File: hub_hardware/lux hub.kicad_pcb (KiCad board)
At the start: 4 copper layers, 105.4 x 54.6 mm, 136 parts, among them CON1 48V, CON2 USB-MINI-B, P1 CONN_4, P2 CONN_4, P3 CONN_4, P4 CONN_4, P5 CONN_4, P6 CONN_4, P7 CONN_4, Q1 DMP6023LE-13, Q10 BC856BLT, Q11 BTX54CTU, Q12 BC856BLT, Q13 BTX54CTU, Q2 BC856BLT, Q3 BTX54CTU, Q4 BC856BLT, Q5 BTX54CTU, Q6 BC856BLT, Q7 BTX54CTU, Q8 BC856BLT, Q9 BTX54CTU, SW1 BOOT, U1 3V3REG, U10 ISL83485IBZ, U11 2CH-TVS, U12 ISL83485IBZ, U13 2CH-TVS, U14 ISL83485IBZ, U15 2CH-TVS, U2 STM32F042-32, U3 4068, U4 ISL83485IBZ, U5 2CH-TVS, U6 ISL83485IBZ, U7 2CH-TVS, U8 ISL83485IBZ, U9 2CH-TVS

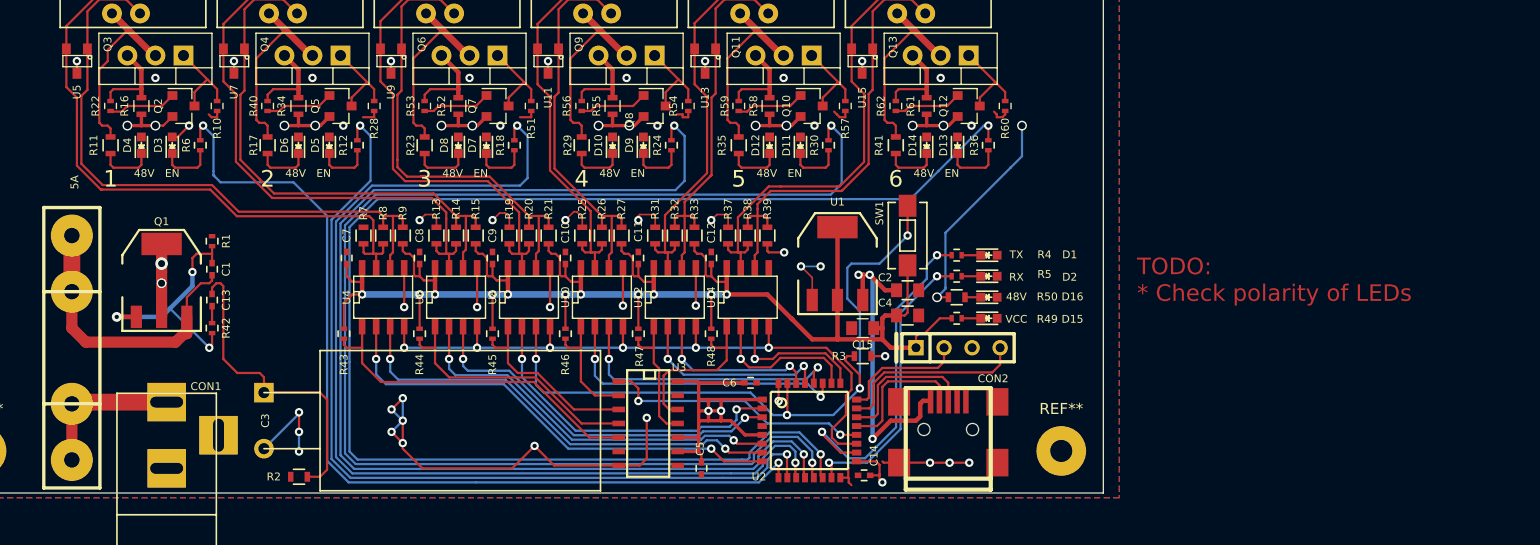
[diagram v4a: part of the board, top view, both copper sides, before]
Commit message: WIP Lux Hub v7; need to re-route 1W 2512 resistors
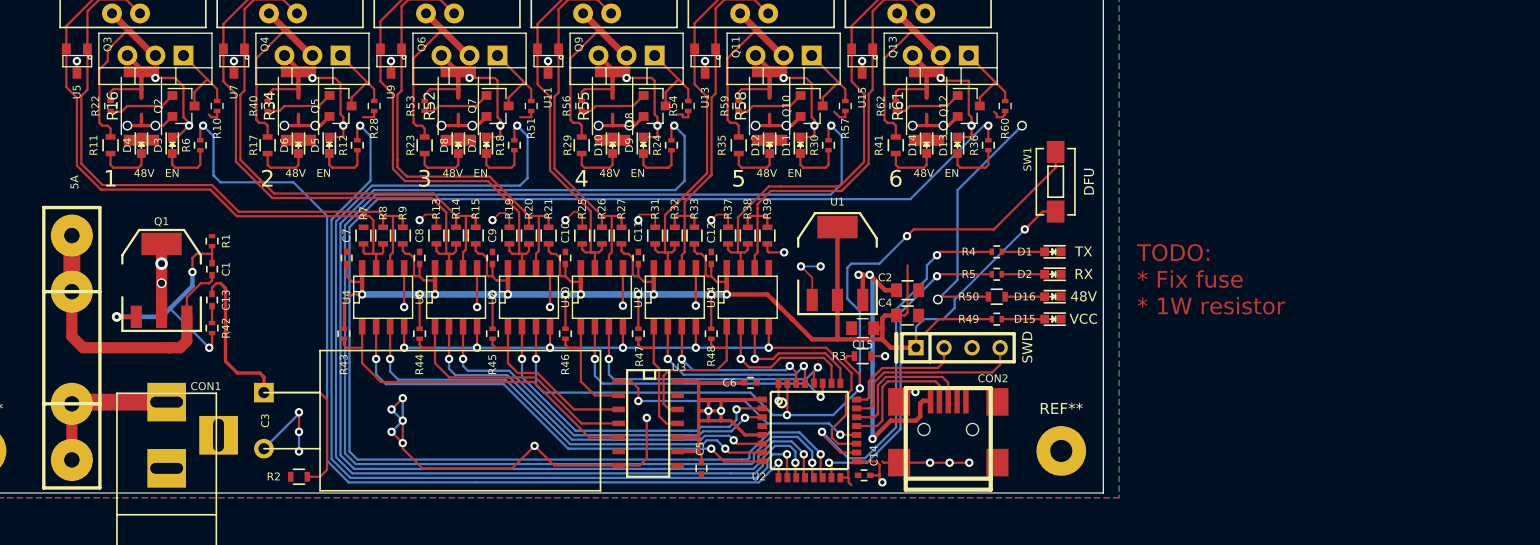
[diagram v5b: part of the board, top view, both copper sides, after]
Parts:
- D1, D10, D11, D12, D13, D14, D15, D16, D2, D3, D4, D5, D6, D7, D8, D9: footprint LEDs:LED_0603 -> custom:LED_0603_flipped
- R16, R34, R52, R55, R58, R61: footprint Resistors_SMD:R_0603 -> Resistors_SMD:R_2512
- moved SW1 14.3 mm to (125.2, 96.3)
- moved D1 5.80 mm to (125.0, 102.6)
- moved D2 5.79 mm to (125.0, 104.6)
- moved D15 5.79 mm to (125.0, 108.7)
- moved D16 5.79 mm to (125.0, 106.7)
- moved R4 3.64 mm to (119.9, 102.6)
- moved R5 3.64 mm to (119.9, 104.6)
- moved R49 3.63 mm to (119.9, 108.7)
- moved R50 3.63 mm to (119.9, 106.7)
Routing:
- net GND: track 117.3 -> 171.5 mm, vias 34 -> 46
- net VCC: track 195.7 -> 218.6 mm, vias 15 -> 16
- net /DE3: track 64.6 -> 79.3 mm
- net +48V: track 90.5 -> 94.3 mm
- net /TX_LED: track 31.4 -> 35.1 mm
- net /RX_LED: track 25.7 -> 29.4 mm
- net Net-(D2-Pad1): track 1.98 -> 3.88 mm
- net Net-(D15-Pad1): track 1.98 -> 3.88 mm
- net Net-(D1-Pad1): track 1.98 -> 3.88 mm
- net Net-(D16-Pad1): track 1.68 -> 3.58 mm
- net Net-(C1-Pad1): track 26.9 -> 27.6 mm
- net (no net): vias 11 -> 0
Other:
- board text added: "DFU"
- board text added: "SWD"
- board text added: "TODO: * Fix fuse * 1W resistor"
- board text removed: "TODO: * Check polarity of LEDs"

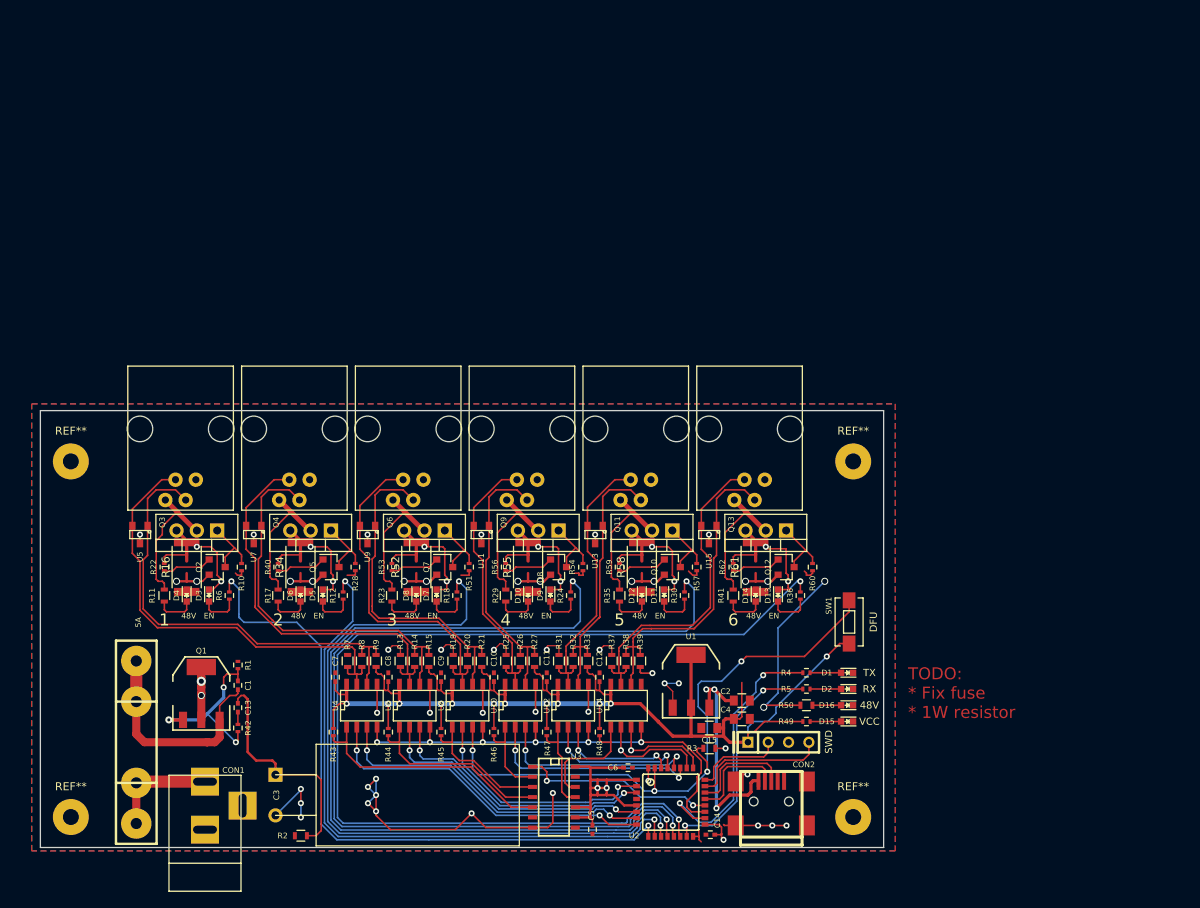
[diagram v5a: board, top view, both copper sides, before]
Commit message: WIP Lux Hub v7; proposed re-route
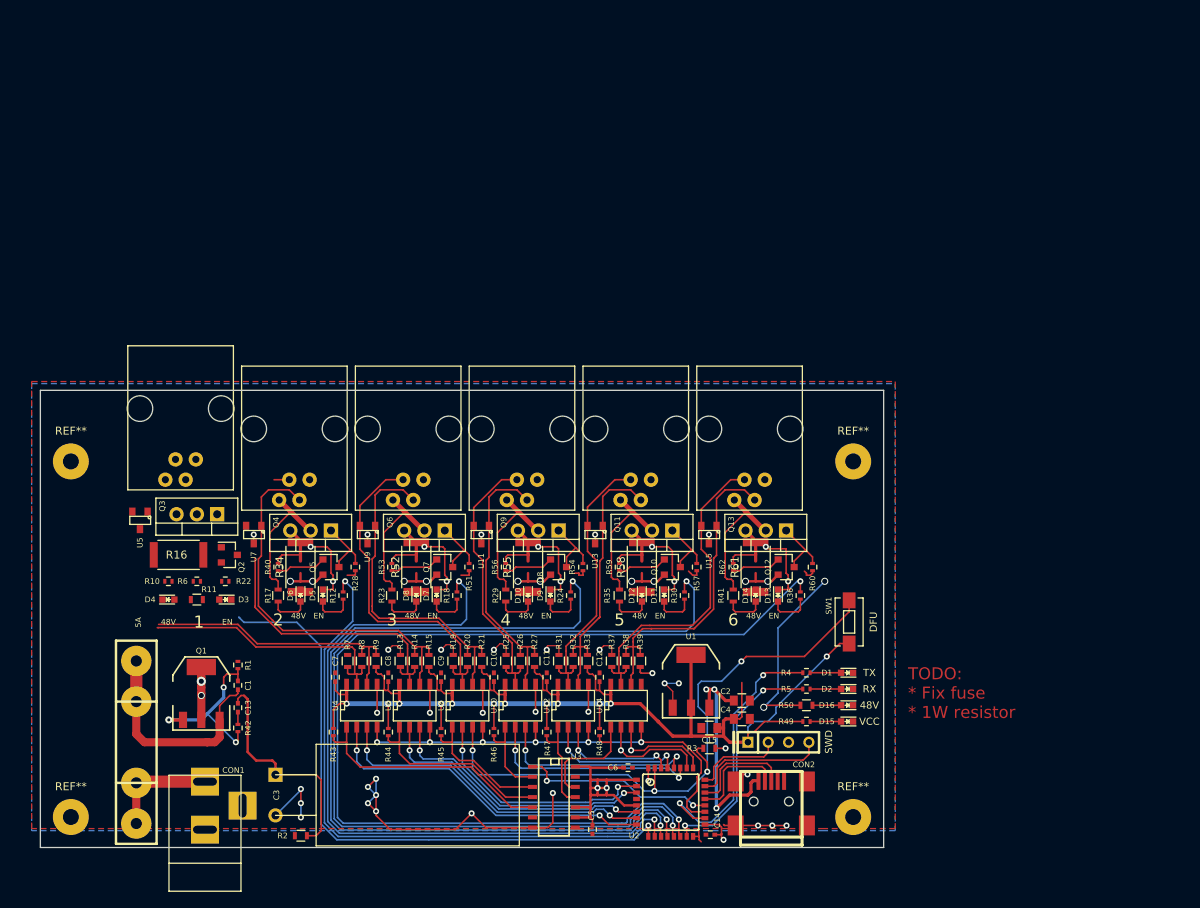
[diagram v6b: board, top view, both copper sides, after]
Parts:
- moved R10 9.32 mm to (40.1, 91.2), turned to 0 degrees
- moved R22 7.82 mm to (47.2, 91.2), turned to 180 degrees
- moved R6 4.44 mm to (43.7, 91.2), turned to 0 degrees
- moved R11 4.10 mm to (43.7, 93.5), turned to 180 degrees
- moved P1 2.54 mm to (41.7, 69.6)
- moved D4 2.34 mm to (40.1, 93.5), turned to 180 degrees
- moved Q2 2.16 mm to (47.8, 87.9)
- moved D3 2.09 mm to (47.2, 93.5), turned to 0 degrees
- moved Q3 2.03 mm to (46.2, 82.8)
- moved R16 1.83 mm to (41.4, 87.9), turned to 180 degrees
- moved U5 1.78 mm to (36.6, 83.6)
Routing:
- net /Port1/dB: track 56.6 -> 33.6 mm
- net /Port1/dA: track 57.6 -> 35.1 mm
- net /Port1/P48: track 17.0 -> 0.00 mm
- net /Port2/dB: track 49.1 -> 37.4 mm
- net GND: track 171.5 -> 160.4 mm, vias 46 -> 43
- net Net-(Q2-Pad3): track 8.28 -> 0.00 mm
- net Net-(Q3-Pad3): track 8.07 -> 0.00 mm
- net /LED1: track 84.2 -> 77.9 mm, vias 2 -> 1
- net Net-(Q2-Pad1): track 6.23 -> 0.00 mm
- net +48V: track 94.3 -> 88.9 mm, vias 16 -> 14
- net Net-(D3-Pad1): track 5.11 -> 0.00 mm
- net Net-(D4-Pad1): track 5.06 -> 0.00 mm
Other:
- board size 105.4 x 54.6 mm -> 105.4 x 57.1 mm

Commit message: Lux Hub v7 (done)
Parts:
- moved D4 8.64 mm to (48.8, 93.5), turned to 90 degrees
- moved D3 7.62 mm to (39.6, 93.5), turned to 90 degrees
- moved R10 7.12 mm to (47.2, 90.9)
- moved D12 6.37 mm to (105.7, 93.5)
- moved D14 6.37 mm to (119.9, 93.5)
- moved D10 6.37 mm to (91.4, 93.5)
- moved D6 6.37 mm to (63.0, 93.5)
- moved REF** 6.14 mm to (126.5, 70.1)
- moved R17 6.12 mm to (59.9, 93.5)
- moved R23 6.12 mm to (74.2, 93.5)
- moved R35 6.12 mm to (102.6, 93.5)
- moved R41 6.12 mm to (116.8, 93.5)
- moved REF** 6.12 mm to (27.4, 70.1)
- moved D8 6.12 mm to (77.2, 93.5)
- moved R29 6.12 mm to (88.4, 93.5)
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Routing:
- net GND: track 160.4 -> 115.4 mm, vias 43 -> 40
- net /Port1/dA: track 35.1 -> 60.7 mm
- net /Port1/dB: track 33.6 -> 59.1 mm
- net /Port1/P48: track 0.00 -> 20.3 mm
- net /Port2/dB: track 37.4 -> 51.4 mm
- net +48V: track 88.9 -> 102.6 mm, vias 14 -> 15
- net Net-(Q2-Pad1): track 0.00 -> 11.6 mm
- net Net-(Q3-Pad3): track 0.00 -> 11.0 mm
- net Net-(Q2-Pad3): track 0.00 -> 9.94 mm
- net /LED1: track 77.9 -> 86.9 mm, vias 1 -> 2
- net /LED4: track 107.2 -> 99.2 mm
- net /LED5: track 121.4 -> 113.4 mm
- net /LED3: track 93.1 -> 85.3 mm
- net Net-(Q8-Pad1): track 6.18 -> 11.8 mm
- net Net-(Q6-Pad1): track 6.18 -> 11.6 mm
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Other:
- board text added: "12V-48V, 5A"
- board text added: "5A Fuse"
- board text added: "Lux Hub rev 7"
- board text added: "Lux Hub rev 7 https://github.com/ervanalb/lux"
- board text added: "https://github.com/ervanalb/lux"
- board text removed: "Lux Hub rev 7 github.com/ervanalb/lux"
- board text removed: "TODO: * Fix fuse * 1W resistor"

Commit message: Export hub gebers v7
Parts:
- renumbered REF** to REF
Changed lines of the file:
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@@
   (module Wire_Pads:SolderWirePad_single_2mmDrill (layer F.Cu)
     (at 27.432 120.904)
-    (fp_text reference REF** (at 0 -3.81) (layer F.SilkS)
+    (fp_text reference REF (at 0 -3.81) (layer F.SilkS) hide
       (effects (font (size 0.71 0.71) (thickness 0.075)))
     )
